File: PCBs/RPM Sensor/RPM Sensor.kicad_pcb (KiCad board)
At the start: 2 copper layers, 39.4 x 40 mm, 23 parts, among them J1 I, J10 DO/DO, J11 SEL/SEL, J12 I, J13 I, J14 I, J15 I, J16 I, J2 B, J3 I, J4 A, J5 U, J6 V, J7 W/PWM, J8 SCL/CLK, J9 NSL/DI, U1 MAG_ENCODER_AEAT-8800-Q24

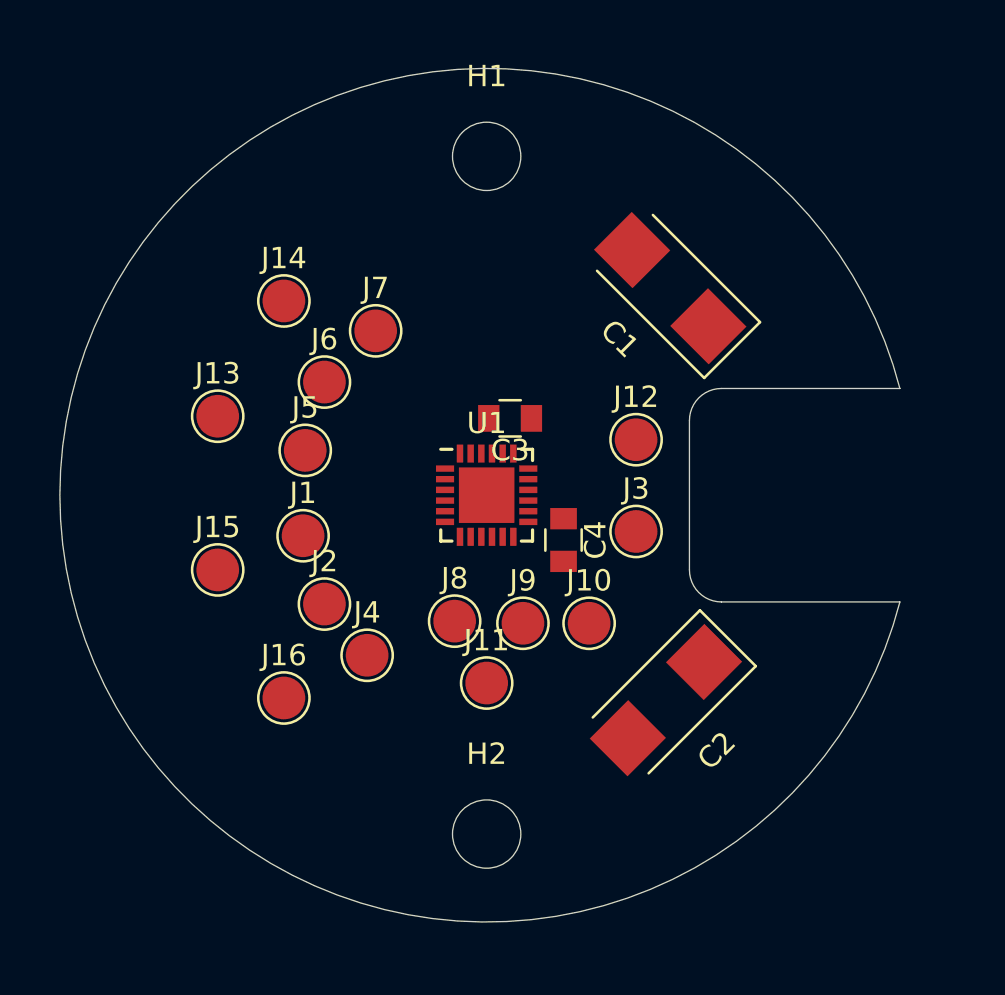
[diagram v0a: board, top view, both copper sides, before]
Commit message: PCB Design Complete
- Updated silkscreen
- Small layout/routing changes
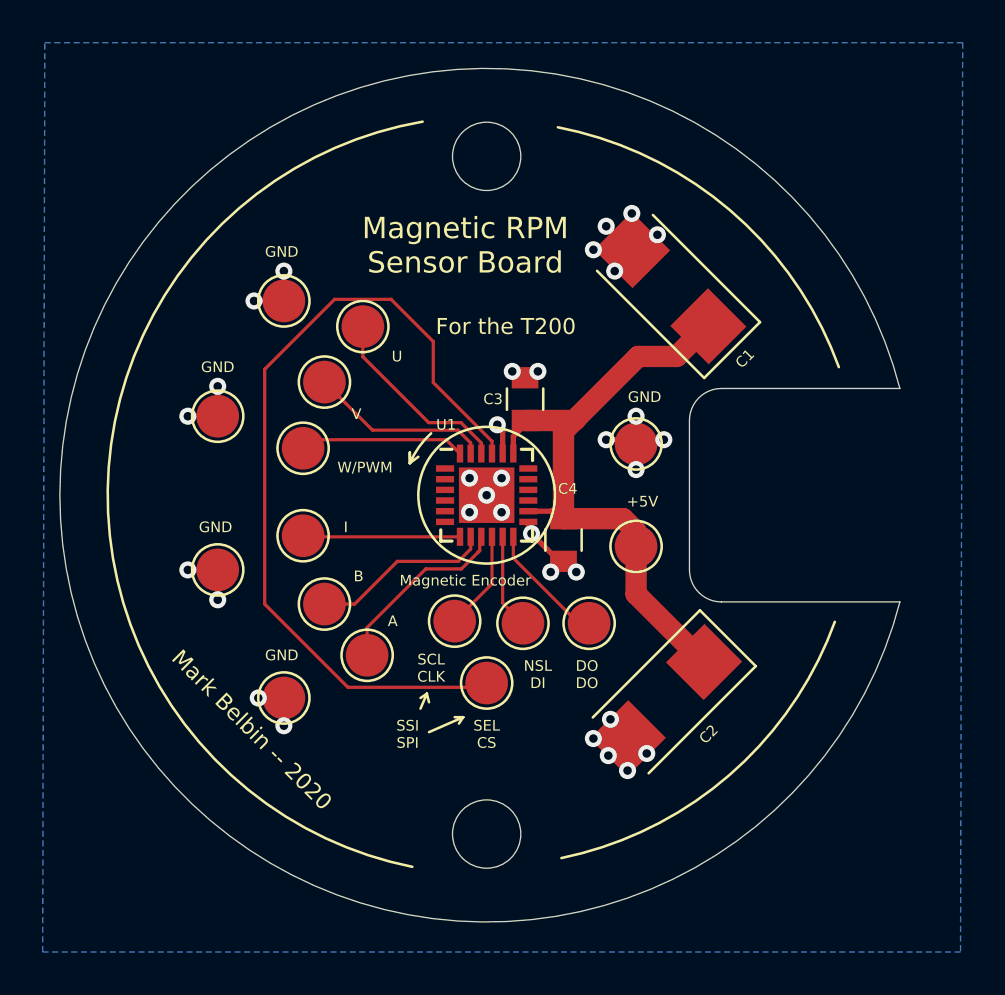
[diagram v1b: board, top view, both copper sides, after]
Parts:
- moved J7 6.47 mm to (91.4, 97.8)
- moved J5 6.40 mm to (94.2, 92.1)
- moved C3 1.14 mm to (101.8, 95.5), turned to 90 degrees
- moved J3 0.70 mm to (107.0, 102.4)
- moved J12 0.20 mm to (107.0, 97.6)
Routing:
- net Net-(J11-Pad1): track 0.00 -> 39.6 mm
- net +5V: track 0.00 -> 30.3 mm
- net GND: track 0.00 -> 22.3 mm, vias 0 -> 33
- net Net-(J5-Pad1): track 0.00 -> 9.14 mm
- net Net-(J4-Pad1): track 0.00 -> 8.80 mm
- net Net-(J6-Pad1): track 0.00 -> 8.53 mm
- net Net-(J2-Pad1): track 0.00 -> 8.49 mm
- net Net-(J7-Pad1): track 0.00 -> 7.78 mm
- net Net-(J1-Pad1): track 0.00 -> 7.37 mm
- net Net-(J10-Pad1): track 0.00 -> 5.81 mm
- net Net-(J8-Pad1): track 0.00 -> 4.67 mm
- net Net-(J9-Pad1): track 0.00 -> 4.44 mm
- added copper zone on B.Cu, net GND
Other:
- rule trace_min: 0.2 -> 0.127
- rule via_min_size: 0.4 -> 0.3
- board text added: "+5V"
- board text added: "A"
- board text added: "B"
- board text added: "DO DO"
- board text added: "For the BR T200"
- board text added: "For the T200"
- board text added: "GND"
- board text added: "I"
- board text added: "Magnetic Encoder"
- board text added: "Magnetic RPM Sensor Board"
- board text added: "Mark Belbin -- 2020"
- board text added: "NSL DI"
- board text added: "SCL CLK"
- board text added: "SEL CS"
- board text added: "SSI SPI"
- board text added: "U"
- board text added: "V"
- board text added: "W/PWM"
